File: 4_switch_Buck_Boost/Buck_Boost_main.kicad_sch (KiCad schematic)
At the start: 98 parts, among them J1 Conn_02x02_Counter_Clockwise, J2 Screw_Terminal_2x5.08, J3 Screw_Terminal_2x2.54, J4 Screw_Terminal_2x5.08, M1 Fan, Q1 CSD18532Q5B, Q101 2N7002K, Q103 BSS83P, Q2 CSD18532Q5B, Q3 CSD18532Q5B, Q4 CSD18532Q5B, Q6 AO3400A, U1 LT8390EUFD_PBF

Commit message: Starting point for PCB Template Transformation
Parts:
- removed M1: Fan, Connector_Molex:Molex_KK-396_5273-02A_1x02_P3.96mm_Vertical, symbol Motor:Fan
- removed Q6: AO3400A, Package_TO_SOT_SMD:SOT-23, symbol Transistor_FET:AO3400A
- removed R4: 100K, rsx_resistors:R_0603_1608Metric, symbol Device:R
- removed R5: 10k, rsx_resistors:R_0603_1608Metric, symbol Device:R
- removed R6: 100, rsx_resistors:R_0603_1608Metric, symbol Device:R
- removed TH1: 10k, Connector_Molex:Molex_KK-396_5273-02A_1x02_P3.96mm_Vertical, symbol rsx_sensors:NTCALUG54A103G351A
- C6, C7: footprint rsx_capacitors:C_0805_2012Metric -> rsx_capacitors:C_0603_1608Metric
- L1: value 15u -> ~; footprint Inductor_SMD:L_Wuerth_WE-XHMI-8080 -> Inductor_SMD:L_Wuerth_WE-PD-Typ-LS
- R103: value 200k -> 10k
- R7: value 6m -> ~
- R8: value 15m -> ~
- RV102: value 50k -> 1M
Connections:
- net SW1: now also R7.3; no longer R7.2
- net at L1.1: now also R7.2; no longer R7.3
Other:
- note added: "Adjusted for En/UVLO ~ Cannot recieve 24V directly ~1.3V Now -- Works for template"
- note added: "FB List -- 5V : (40k+10k)/10k OVP: 5.5V SCT: 1.25V 12V : (110k+10k)/10k OVP: 13.2V SCT: 3.0V 24V : (230k+10k)/10k OVP: 26.4V SCT: 6.0V 55V : (540k+10k)/10k OVP: 60.5V SCT: 13.75V ----------"
- note removed: "Adjusted for En/UVLO ~ Cannot recieve 24V directly ~1.3V Now"
- note removed: "FB: 24V : ((200k+30k)+10k)/10k"
- note removed: "Fan Control Using Heat Probe"
- note removed: "NTC FAN PORT CONTROL"
- moved on the sheet: C5, R103, R104, R7, RV102, TP6

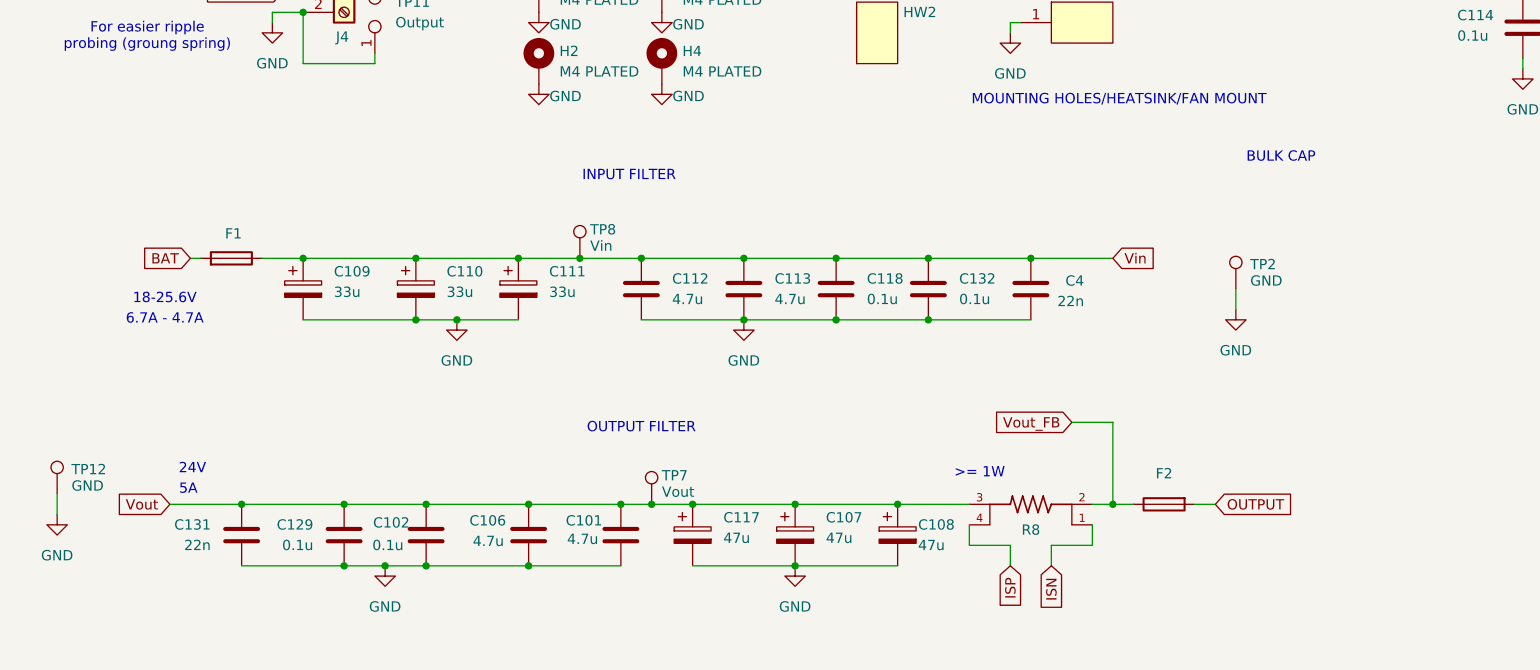
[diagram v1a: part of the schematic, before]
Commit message: reverse polarity protection
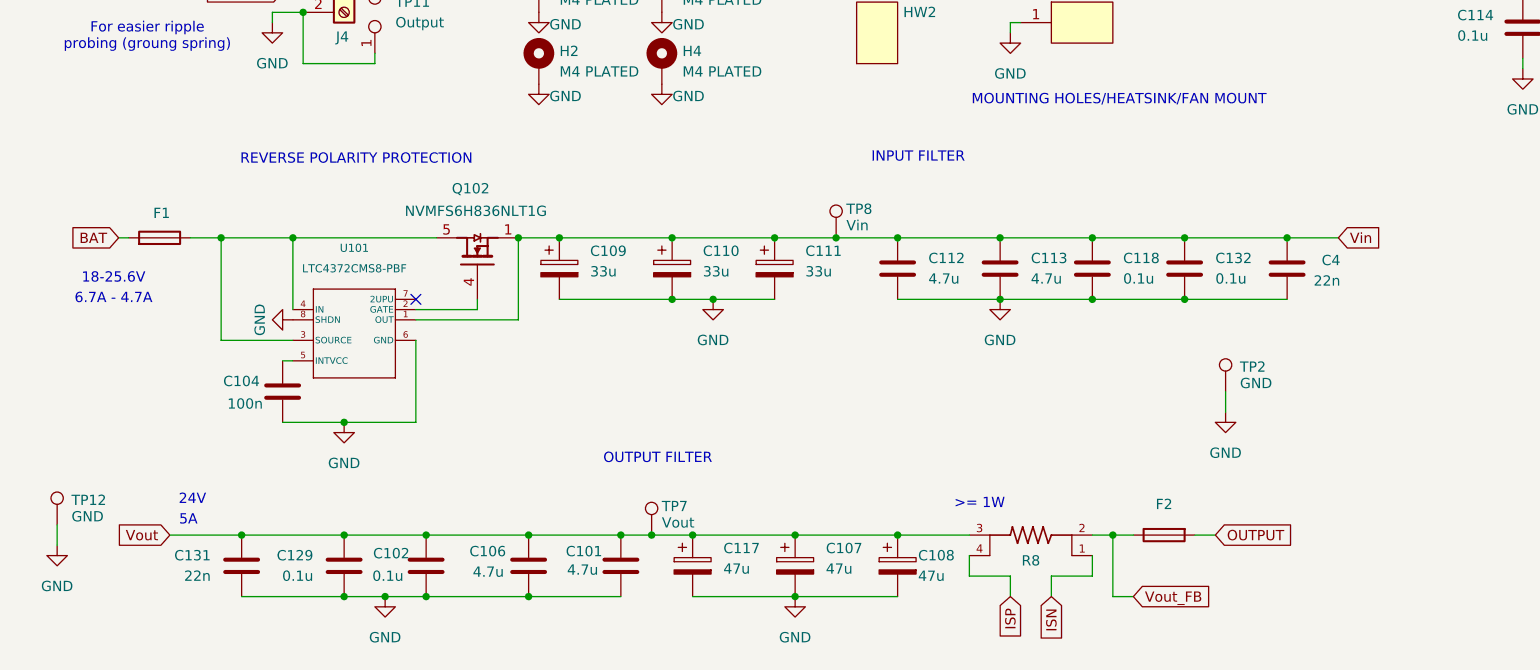
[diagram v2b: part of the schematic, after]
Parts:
- added C104: 100n, rsx_capacitors:C_0603_1608Metric, symbol Device:C
- added Q102: NVMFS6H836NLT1G, Package_SO:ONSemi_SO-8FL_488AA, symbol NVMFS6H836NL:NVMFS6H836NLT1G
- added U101: LTC4372CMS8-PBF, MS8_05-08-1660_ADI, symbol LTC4372:LTC4372CMS8-PBF
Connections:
- net GND: now also C104.2, U101.6 (GND), U101.8 (SHDN)
- net Vin: now also Q102.1 (S), Q102.2 (S), Q102.3 (S), U101.1 (OUT); no longer F1.2
- new net: Q102.4 (G), U101.2 (GATE)
- new net: F1.2, Q102.5 (D), U101.3 (SOURCE), U101.4 (IN)
- new net: C104.1, U101.5 (INTVCC)
- no-connect marks 2 -> 3
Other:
- note added: "REVERSE POLARITY PROTECTION"
- note removed: "BULK CAP"
- moved on the sheet: C101, C102, C106, C107, C108, C109, C110, C111, C112, C113, C117, C118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

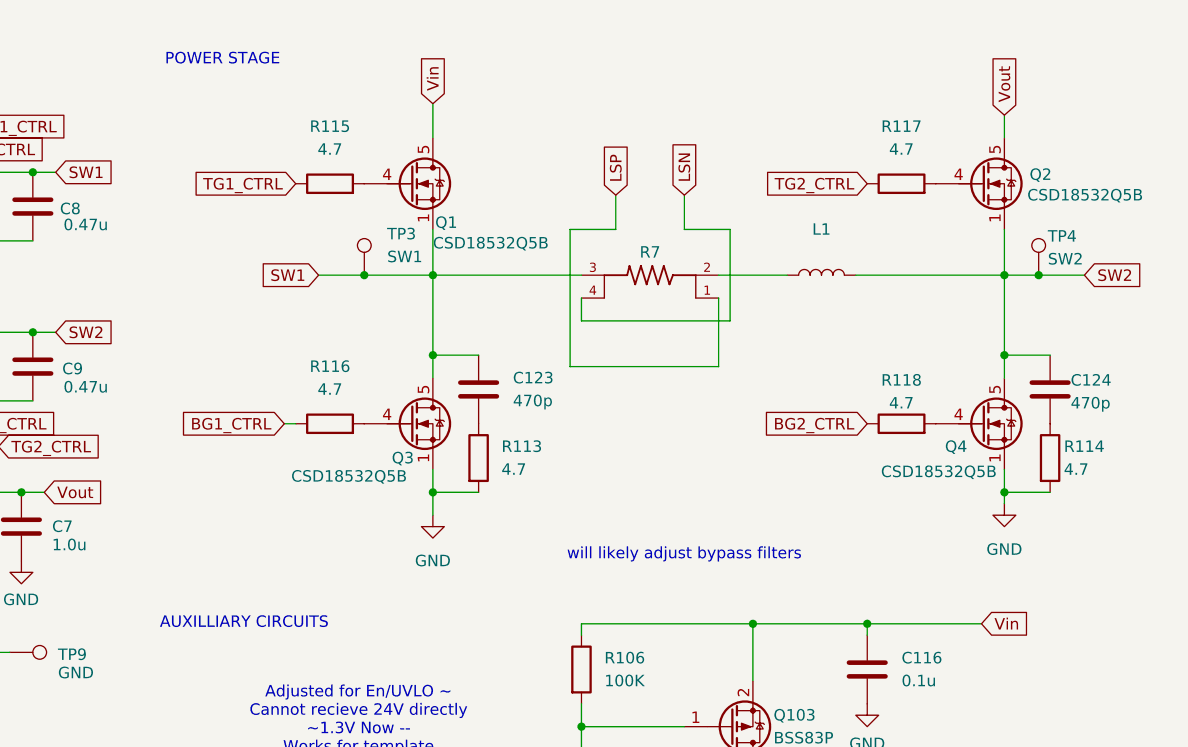
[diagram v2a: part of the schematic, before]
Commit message: Latest FET and Inductor update, Connected Analog traces
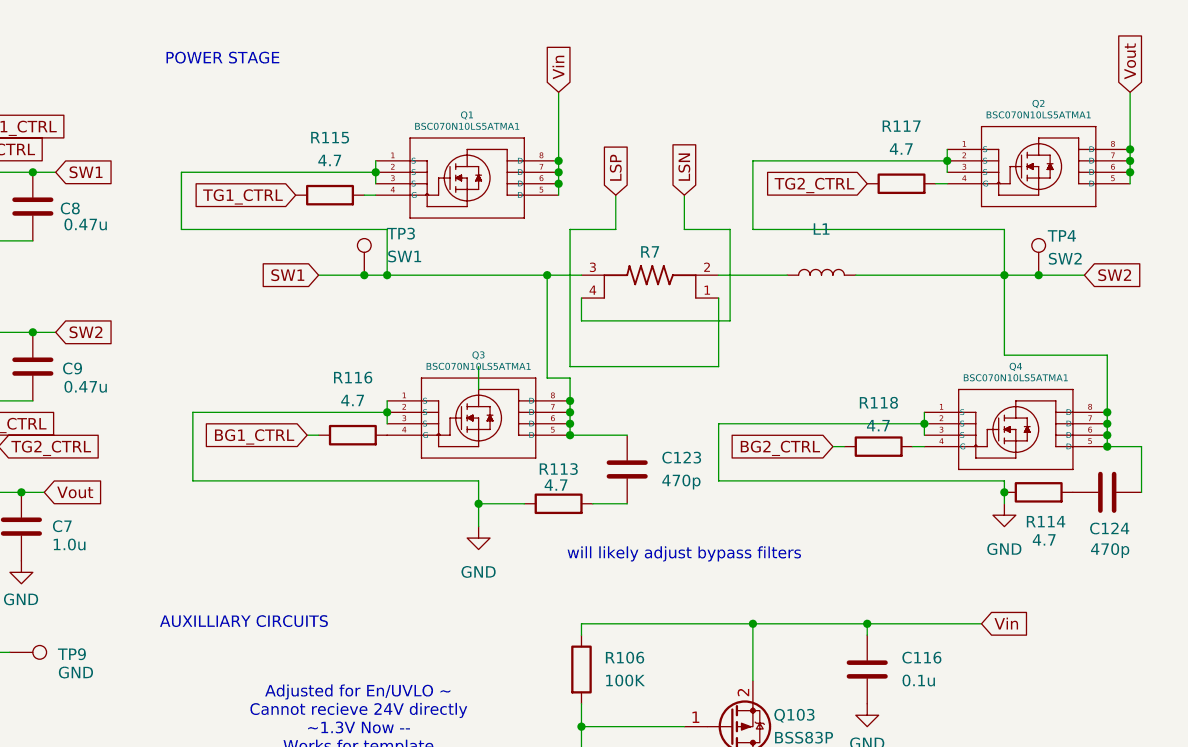
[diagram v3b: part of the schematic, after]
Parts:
- removed Q1, Q2, Q3, Q4: CSD18532Q5B, Package_TO_SOT_SMD:TDSON-8-1, symbol Transistor_FET:CSD18532Q5B
- added Q1, Q3, Q4: BSC070N10LS5ATMA1, Infineon BSC070:PG-TDSON-8-7_INF, symbol Infineon BSC070_medium:BSC070N10LS5ATMA1
- added Q2: BSC070N10LS5ATMA1, PG-TDSON-8-7_INF, symbol Infineon BSC070_medium:BSC070N10LS5ATMA1
- L1: footprint Inductor_SMD:L_Wuerth_WE-PD-Typ-LS -> Inductor_SMD:L_Bourns_SRP1770TA_16.9x16.9mm
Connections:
- net GND: now also R113.1, R114.1, Q3.1 (S), Q3.2 (S), Q3.3 (S), Q4.1 (S), Q4.2 (S), Q4.3 (S); no longer R113.2, R114.2
- net SW1: now also Q1.1 (S), Q1.2 (S), Q1.3 (S), Q3.5 (D), Q3.6 (D), Q3.7 (D), Q3.8 (D)
- net SW2: now also C124.2, Q2.1 (S), Q2.2 (S), Q2.3 (S), Q4.5 (D), Q4.6 (D), Q4.7 (D), Q4.8 (D); no longer C124.1
- net Vin: now also Q1.5 (D), Q1.6 (D), Q1.7 (D), Q1.8 (D)
- net Vout: now also Q2.5 (D), Q2.6 (D), Q2.7 (D), Q2.8 (D)
- net at R116.2: now also Q3.4 (G)
- net at C123.2: now also R113.2; no longer R113.1
- net at R118.2: now also Q4.4 (G)
- net at R115.2: now also Q1.4 (G)
- net at R117.2: now also Q2.4 (G)
- new net: C124.1, R114.2
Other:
- moved on the sheet: C123, C124, R113, R114, R115, R116, R118

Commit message: Rsense footprint changes
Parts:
- R7, R8: footprint shunt:RES_KRL3216T4-M-R003-F-T1 -> Rsense_Littelfuse_L4CL:R_2512_4Pad_Littelfuse_L4CL
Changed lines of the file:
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@@
 			)
 		)
-		(property "Footprint" "shunt:RES_KRL3216T4-M-R003-F-T1"
+		(property "Footprint" "Rsense_Littelfuse_L4CL:R_2512_4Pad_Littelfuse_L4CL"
 			(at 227.33 41.91 0)
 			(effects
@@
 			)
 		)
-		(property "Footprint" "shunt:RES_KRL3216T4-M-R003-F-T1"
+		(property "Footprint" "Rsense_Littelfuse_L4CL:R_2512_4Pad_Littelfuse_L4CL"
 			(at 149.86 184.15 0)
 			(effects

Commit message: correct resistor footprint
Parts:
- R7: footprint Rsense_Littelfuse_L4CL:R_2512_4Pad_Littelfuse_L4CL -> Littelfuse_L4CA0612_KiCad9:Littelfuse_L4CA0612_4Terminal
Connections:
- net LSN: now also R7.1; no longer R7.4
- net LSP: now also R7.4; no longer R7.1
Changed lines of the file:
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@@
 	(wire
 		(pts
-			(xy 231.14 33.02) (xy 231.14 36.83)
-		)
-		(stroke
-			(width 0)
-			(type default)
-		)
-	)
-	(wire
-		(pts
 			(xy 153.67 83.82) (xy 153.67 86.36)
 		)
@@
 	(wire
 		(pts
-			(xy 236.22 46.99) (xy 219.71 46.99)
-		)
-		(stroke
-			(width 0)
-			(type default)
-		)
-	)
-	(wire
-		(pts
 			(xy 278.13 60.96) (xy 281.94 60.96)
 		)
@@
 	(wire
 		(pts
-			(xy 218.44 36.83) (xy 223.52 36.83)
-		)
-		(stroke
-			(width 0)
-			(type default)
-		)
-	)
-	(wire
-		(pts
 			(xy 218.44 58.42) (xy 218.44 59.69)
 		)
@@
 	(wire
 		(pts
-			(xy 231.14 36.83) (xy 236.22 36.83)
-		)
-		(stroke
-			(width 0)
-			(type default)
-		)
-	)
-	(wire
-		(pts
 			(xy 87.63 68.58) (xy 97.79 68.58)
 		)
@@
 	(wire
 		(pts
-			(xy 234.95 52.07) (xy 234.95 44.45)
-		)
-		(stroke
-			(width 0)
-			(type default)
-		)
-	)
-	(wire
-		(pts
 			(xy 247.65 60.96) (xy 248.92 60.96)
 		)
@@
 	(wire
 		(pts
-			(xy 223.52 33.02) (xy 223.52 36.83)
-		)
-		(stroke
-			(width 0)
-			(type default)
-		)
-	)
-	(wire
-		(pts
 			(xy 93.98 148.59) (xy 99.06 148.59)
 		)
@@
 	(wire
 		(pts
-			(xy 218.44 52.07) (xy 234.95 52.07)
-		)
-		(stroke
-			(width 0)
-			(type default)
-		)
-	)
-	(wire
-		(pts
 			(xy 74.295 43.815) (xy 73.025 43.815)
 		)
@@
 	(wire
 		(pts
-			(xy 218.44 36.83) (xy 218.44 52.07)
-		)
-		(stroke
-			(width 0)
-			(type default)
-		)
-	)
-	(wire
-		(pts
 			(xy 266.7 41.91) (xy 266.7 50.8)
 		)
@@
 	(wire
 		(pts
+			(xy 234.95 44.45) (xy 234.95 46.99)
+		)
+		(stroke
+			(width 0)
+			(type default)
+		)
+	)
+	(wire
+		(pts
 			(xy 40.64 177.8) (xy 53.34 177.8)
 		)
@@
 	(wire
 		(pts
-			(xy 236.22 36.83) (xy 236.22 46.99)
-		)
-		(stroke
-			(width 0)
-			(type default)
-		)
-	)
-	(wire
-		(pts
 			(xy 62.23 151.13) (xy 74.93 151.13)
 		)
@@
 		)
 	)
-	(global_label "LSP"
-		(shape input)
-		(at 223.52 33.02 90)
-		(fields_autoplaced yes)
-		(effects
-			(font
-				(size 1.27 1.27)
-			)
-			(justify left)
-		)
-		(property "Intersheetrefs" "${INTERSHEET_REFS}"
-			(at 223.52 26.5272 90)
-			(effects
-				(font
-					(size 1.27 1.27)
-				)
-				(justify left)
-				(hide yes)
-			)
-		)
-	)
 	(global_label "BAT"
 		(shape input)
@@
 		)
 	)
-	(global_label "LSN"
+	(global_label "LSP"
 		(shape input)
-		(at 231.14 33.02 90)
+		(at 219.71 46.99 270)
 		(fields_autoplaced yes)
 		(effects
@@
 				(size 1.27 1.27)
 			)
-			(justify left)
+			(justify right)
 		)
 		(property "Intersheetrefs" "${INTERSHEET_REFS}"
-			(at 231.14 26.4667 90)
+			(at 219.71 53.4828 90)
 			(effects
 				(font
 					(size 1.27 1.27)
 				)
-				(justify left)
+				(justify right)
 				(hide yes)
 			)
@@
 		)
 	)
+	(global_label "LSN"
+		(shape input)
+		(at 234.95 46.99 270)
+		(fields_autoplaced yes)
+		(effects
+			(font
+				(size 1.27 1.27)
+			)
+			(justify right)
+		)
+		(property "Intersheetrefs" "${INTERSHEET_REFS}"
+			(at 234.95 53.5433 90)
+			(effects
+				(font
+					(size 1.27 1.27)
+				)
+				(justify right)
+				(hide yes)
+			)
+		)
+	)
 	(global_label "TG2_CTRL"
 		(shape input)
@@
 			)
 		)
-		(property "Footprint" "Rsense_Littelfuse_L4CL:R_2512_4Pad_Littelfuse_L4CL"
+		(property "Footprint" "Littelfuse_L4CA0612_KiCad9:Littelfuse_L4CA0612_4Terminal"
 			(at 227.33 41.91 0)
 			(effects

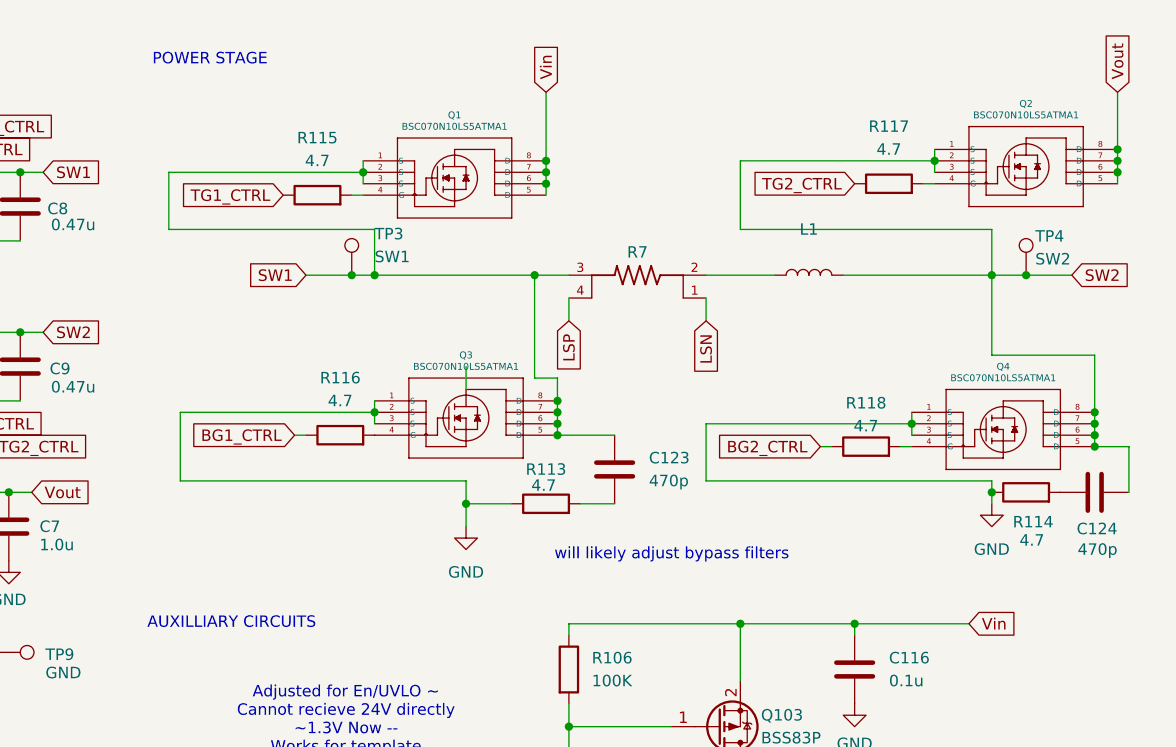
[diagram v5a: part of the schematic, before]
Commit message: MOSFET footprint and symbol update
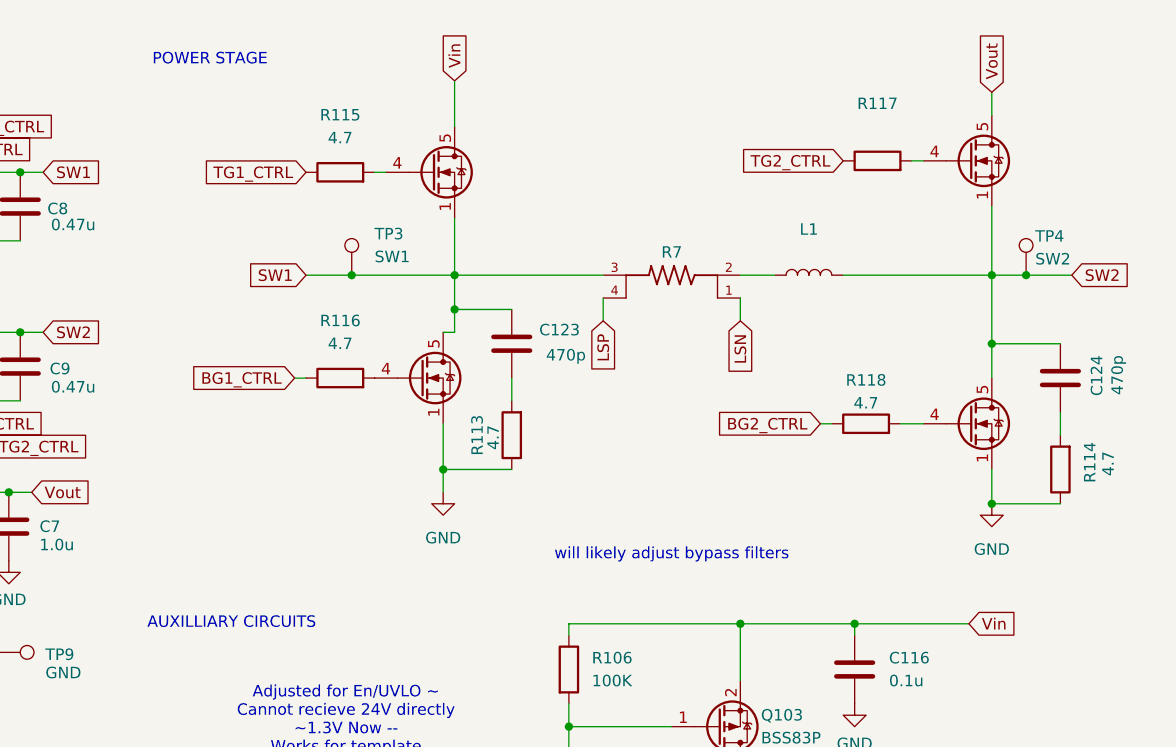
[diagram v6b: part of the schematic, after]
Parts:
- removed Q1, Q3, Q4: BSC070N10LS5ATMA1, Infineon BSC070:PG-TDSON-8-7_INF, symbol Infineon BSC070_medium:BSC070N10LS5ATMA1
- removed Q2: BSC070N10LS5ATMA1, PG-TDSON-8-7_INF, symbol Infineon BSC070_medium:BSC070N10LS5ATMA1
- added Q104, Q105, Q106, Q107: BSC070N10LS5, RSX_TDSON:TDSON-8-1, symbol BSC070N10LS5_MOSFET_STYLE:BSC070N10LS5
- R8: footprint Rsense_Littelfuse_L4CL:R_2512_4Pad_Littelfuse_L4CL -> Littelfuse_L4CA0612_KiCad9:Littelfuse_L4CA0612_4Terminal
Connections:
- net GND: now also Q106.1 (S), Q106.2, Q106.3, Q107.1 (S), Q107.2, Q107.3
- net SW1: now also Q104.1 (S), Q104.2, Q104.3, Q107.5 (D), Q107.6, Q107.7, Q107.8
- net SW2: now also Q105.1 (S), Q105.2, Q105.3, Q106.5 (D), Q106.6, Q106.7, Q106.8
- net Vin: now also Q104.5 (D), Q104.6, Q104.7, Q104.8
- net Vout: now also Q105.5 (D), Q105.6, Q105.7, Q105.8
- net at R116.2: now also Q107.4 (G)
- net at R118.2: now also Q106.4 (G)
- net at R115.2: now also Q104.4 (G)
- net at R117.2: now also Q105.4 (G)
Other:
- moved on the sheet: C123, C124, R113, R114, R115, R116, R117, R118, R7
